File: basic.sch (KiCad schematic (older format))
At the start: 71 parts, among them CON1 MSATA-PCIE_MINI-CARD-MM60-52B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, J2 simcard, J3 Conn_01x02_Male, J4 Conn_01x02_Male, J5 Conn_02x02_Top_Bottom, Q3 MBT3904DW1, SW1 SW_Push, U1 ESP32-WROOM-32U, U2 MCP2515-QFN, U4 TCAN332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

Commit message: readability
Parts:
- removed C11, C5, C6, C7: 56pf, Capacitor_SMD:C_0603_1608Metric, symbol Device:C
- removed C12, C13: 33pf, Capacitor_SMD:C_0603_1608Metric, symbol Device:C
- removed C15, C2, C35, C40, C41, C42, C43, C44, C45, C46, C49: 10uF, Capacitor_SMD:C_1206_3216Metric, symbol Device:C
- removed C22, C23, C24: 33pF, Capacitors:0603, symbol Device:C
- removed C25: 100nF, Capacitors:0603, symbol Device:C
- removed C27: 4.7uF, Capacitor_SMD:C_0603_1608Metric, symbol Device:C
- removed C28, C29: 0.1uF, Capacitor_SMD:C_0603_1608Metric, symbol Device:C
- removed CON1: MSATA-PCIE_MINI-CARD-MM60-52B1-G1-R850(Digi-Key_P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, OLIMEX_Connectors-FP:MM60-52B1-G1-R850, symbol OLIMEX_Connectors:MSATA-PCIE_MINI-CARD-MM60-52B1-G1-R850(Digi-Key_PN_670-2516-2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
- removed D3: SZNUP2105L, Package_TO_SOT_SMD:SOT-23, symbol Power_Protection:SZNUP2105L
- removed D5: DNP Backup, Diode_SMD:D_SOD-123, symbol Device:D_Schottky
- removed J2: simcard, aep:nanosim-Wurth-693043020611, symbol aep:nanosim
- removed J3: Conn_01x02_Male, Connector_JST:JST_SH_SM02B-SRSS-TB_1x02-1MP_P1.00mm_Horizontal, symbol Connector:Conn_01x02_Male
- removed J4: Conn_01x02_Male, Connector_JST:JST_SH_BM02B-SRSS-TB_1x02-1MP_P1.00mm_Vertical, symbol Connector:Conn_01x02_Male
- removed L2: PE-1210ACC110STS 11UH, aep:PE-1210ACC, symbol aep:PE-1210ACC
- removed R17, R18: 3k6, Resistors:0603, symbol Device:R
- removed R3: 1K-10K, Resistor_SMD:R_0603_1608Metric, symbol Device:R
- removed R5, R6, R7: 45, Resistors:0603, symbol Device:R
- removed TP2: L0, OLIMEX_TestPoints-FP:TP_SMD, symbol Connector:TestPoint_Alt
- removed TP3: L1, OLIMEX_TestPoints-FP:TP_SMD, symbol Connector:TestPoint_Alt
- removed TP4: L3, OLIMEX_TestPoints-FP:TP_SMD, symbol Connector:TestPoint_Alt
- removed U2: MCP2515-QFN, Package_DFN_QFN:QFN-20-1EP_4x4mm_P0.5mm_EP2.5x2.5mm_ThermalVias, symbol aep:MCP2515-QFN
- removed U4: TCAN332, Package_TO_SOT_SMD:SOT-23-8, symbol Interface_CAN_LIN:TCAN332
- removed U6: MIC94085, aep:IC_MIC94080YFT-TR, symbol aep:MIC94080YFT-TR
- removed U7: MMA8452Q, QFN-16, symbol SparkFun-Sensors:MMA8452Q
- removed U8: TPS22810DRV, Package_SON:WSON-6-1EP_2x2mm_P0.65mm_EP1x1.6mm, symbol Power_Management:TPS22810DRV
- removed Y2: M8AIG-16-12-2T3, Crystal:Crystal_SMD_Abracon_ABM8G-4Pin_3.2x2.5mm, symbol SparkFun-Clocks:CRYSTAL-16MHZSMD-5X3.2
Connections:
- no-connect marks 31 -> 8
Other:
- note added: "TODO\n\n- breakout modem signals\n- TI DCDC might need to be set to 3.4V, check datasheets of all the stuff\n- MCP73223 UVLO is too low?\n- OPAMP for sense"
- note removed: "TODO\n\n- more bypass on cpu\n- breakout modem signals\n\n\n- Modem FET is flipped ???? (did flip, but i'm still confused)\n- TI DCDC might need to be set to 3.4V, check datasheets of all the stuff\n- The Hirose BAT connector is terrible, need one with mechanical mounts\n- 12V_SENSE is actually BAT_SENSE. we need a second sense for 12V\n- MCP73223 UVLO is too low?\n- disable mcp on engine off -> 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"
- moved on the sheet: C1, C3, C4, D1, D4, FID1, FID2, J5, Q3A, Q3B, R1, R19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

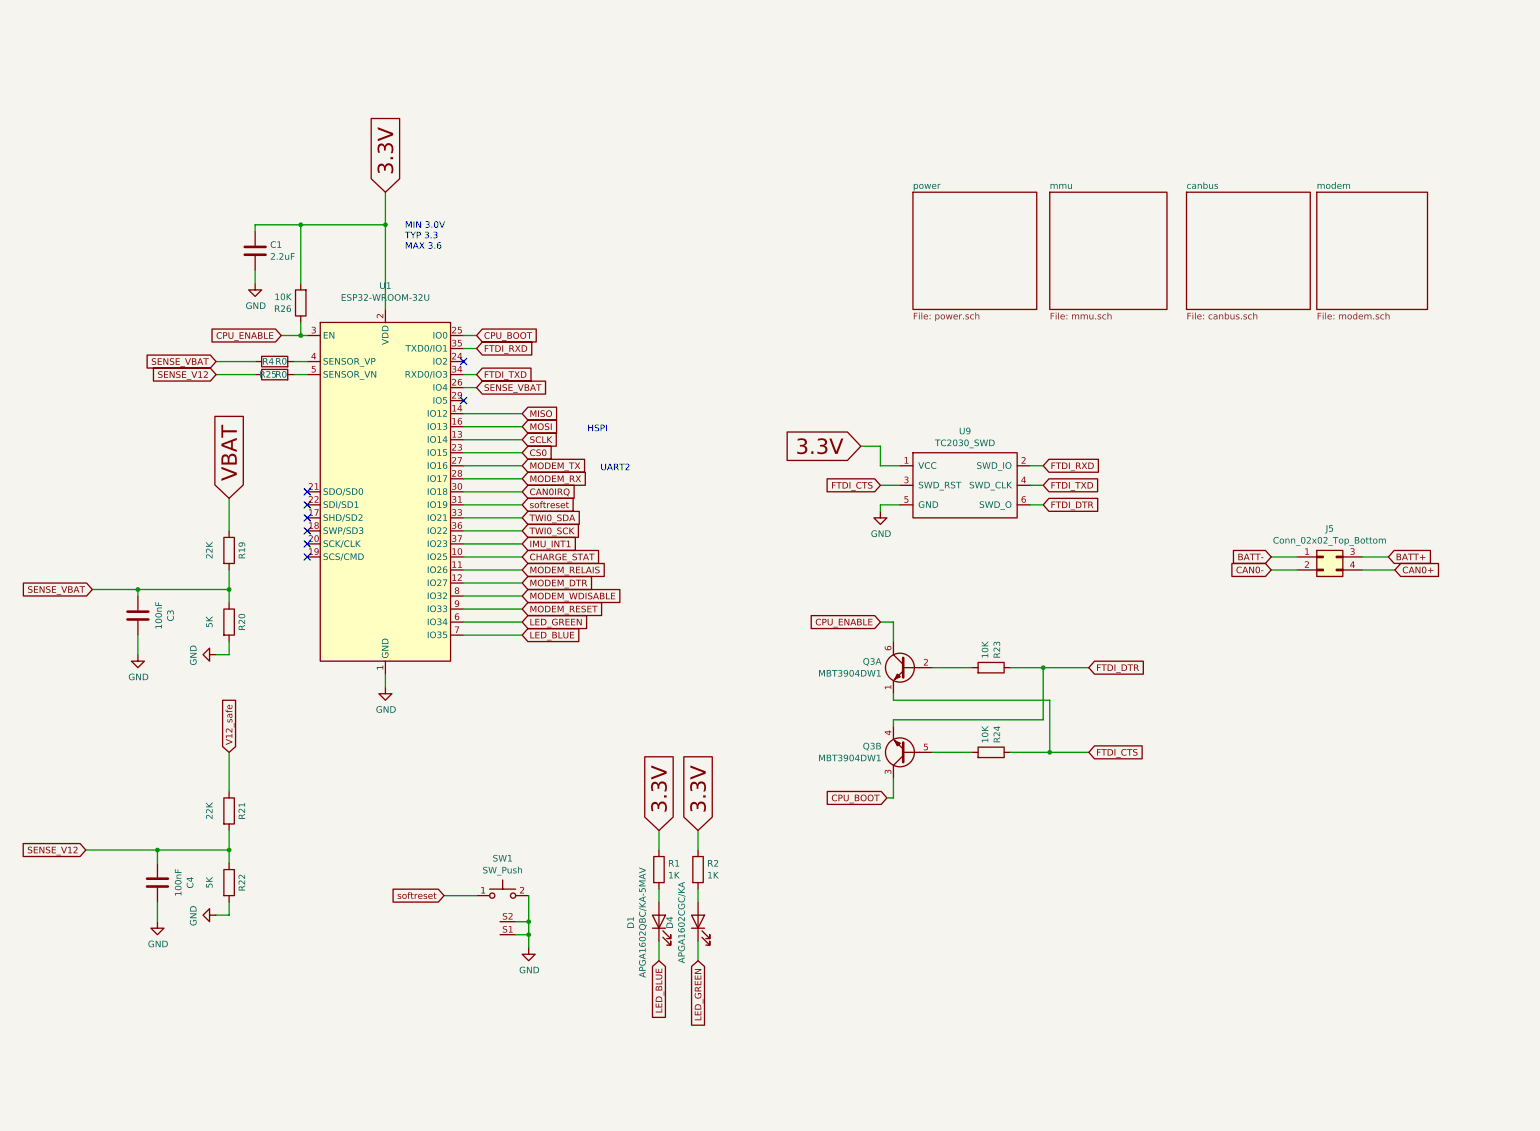
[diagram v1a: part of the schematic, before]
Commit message: MMU Schematic rework.
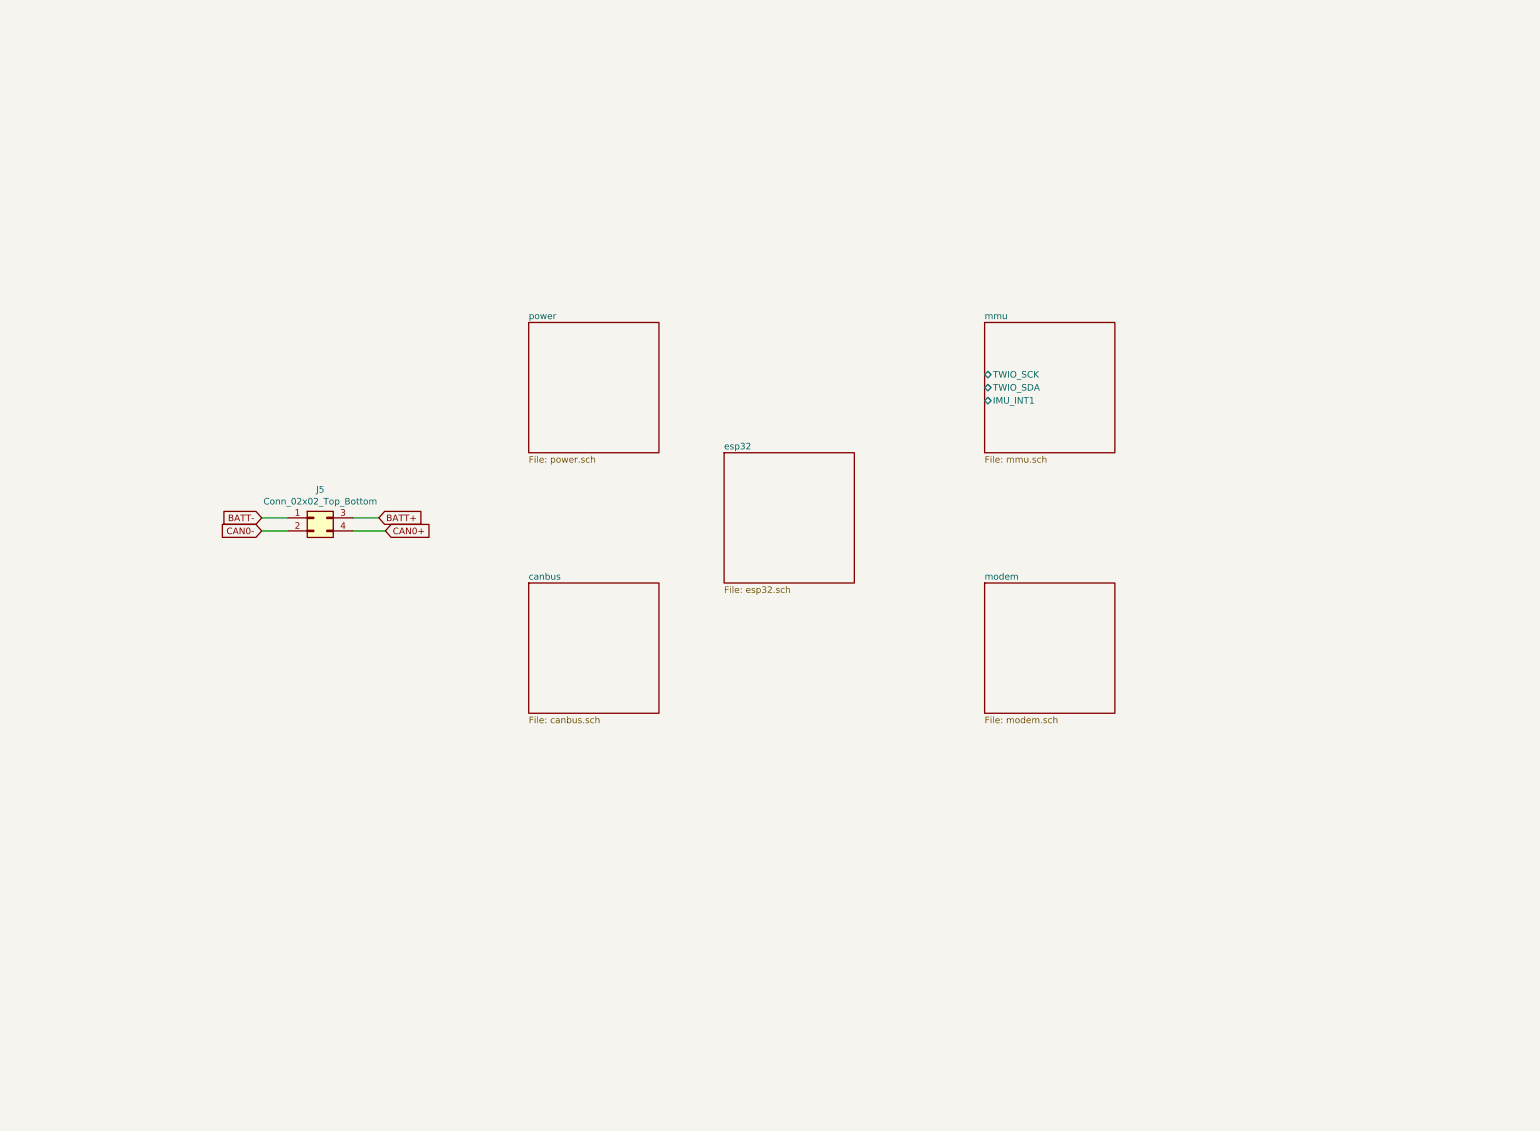
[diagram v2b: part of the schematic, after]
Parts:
- removed C1: 2.2uF, Capacitors:0603, symbol Device:C
- removed C3, C4: 100nF, Capacitor_SMD:C_0603_1608Metric, symbol Device:C
- removed D1: APGA1602QBC/KA-5MAV, LED_SMD:LED_0603_1608Metric, symbol Device:LED
- removed D4: APGA1602CGC/KA, LED_SMD:LED_0603_1608Metric, symbol Device:LED
- removed Q3: MBT3904DW1, Package_TO_SOT_SMD:SOT-363_SC-70-6, symbol Transistor_BJT:MBT3904DW1
- removed R1, R2: 1K, Resistor_SMD:R_0603_1608Metric, symbol Device:R
- removed R19, R21: 22K, Resistors:0603, symbol Device:R
- removed R20, R22: 5K, Resistors:0603, symbol Device:R
- removed R23, R24, R26: 10K, Resistors:0603, symbol Device:R
- removed R25, R4: R0, Resistors:0603, symbol Device:R
- removed SW1: SW_Push, aep:SW_1825027-5, symbol aep:SW_Push
- removed U1: ESP32-WROOM-32U, RF_Module:ESP32-WROOM-32U, symbol RF_Module:ESP32-WROOM-32U
- removed U9: TC2030_SWD, Connector:Tag-Connect_TC2030-IDC-FP_2x03_P1.27mm_Vertical, symbol aep:TC2030_SWD
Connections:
- no-connect marks 8 -> 0
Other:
- note removed: "HSPI"
- note removed: "MIN 3.0V\nTYP 3.3\nMAX 3.6"
- note removed: "UART2"
- moved on the sheet: J5
